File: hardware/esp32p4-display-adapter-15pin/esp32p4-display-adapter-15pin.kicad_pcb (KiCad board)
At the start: 2 copper layers, 20 x 30 mm, 0 parts

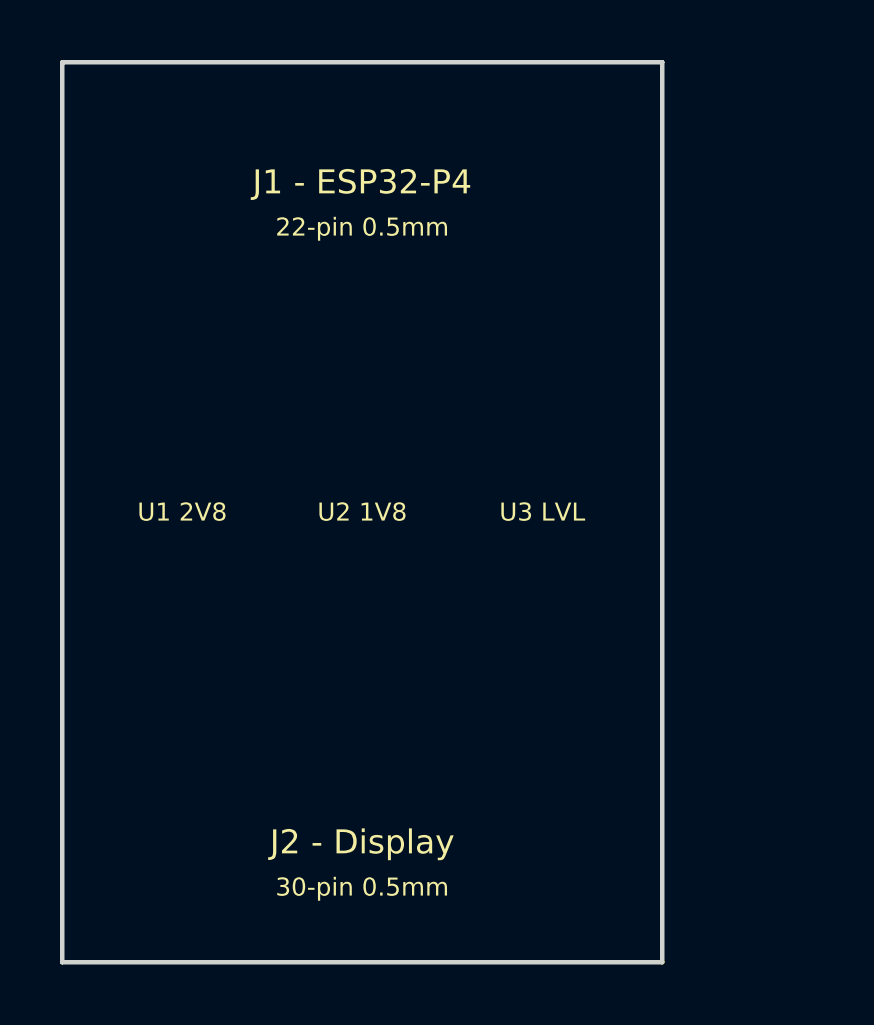
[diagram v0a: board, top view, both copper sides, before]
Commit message: Restore esp32p4-display-adapter (22-pin), add esp32p4-display-adapter-15pin
- esp32p4-display-adapter: 22-pin 0.5mm (your working version restored)
- esp32p4-display-adapter-15pin: NEW - 15-pin 1.0mm (same pinout as RPi)
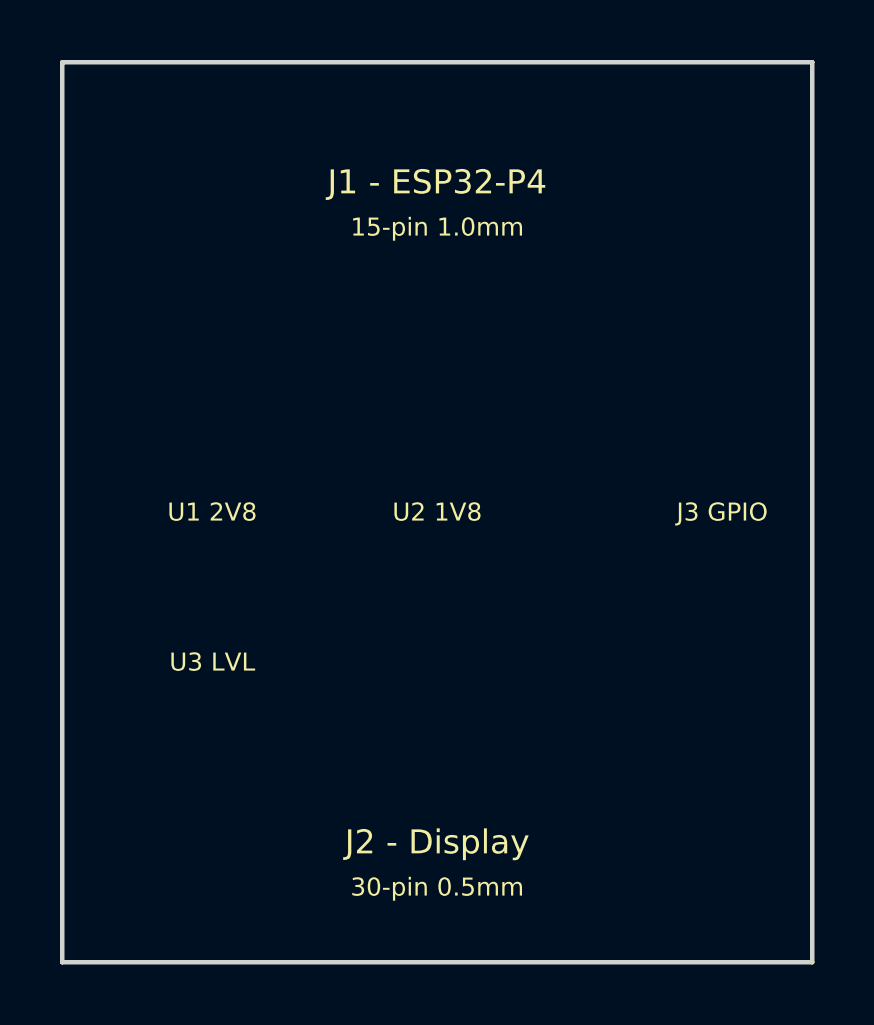
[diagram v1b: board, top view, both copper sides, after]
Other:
- board size 20 x 30 mm -> 25 x 30 mm
- board text added: "15-pin 1.0mm"
- board text added: "J3 GPIO"
- board text removed: "22-pin 0.5mm"
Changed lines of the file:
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@@
   (paper "A4")
   (title_block
-    (title "ESP32-P4 DSI to Round Display Adapter (22-pin)")
+    (title "ESP32-P4 DSI to Round Display Adapter (15-pin)")
     (date "2026-04-24")
     (rev "1.0")
@@
   (net 15 "TP_RESET_3V3")
   (net 16 "TP_RESET_1V8")
-  (net 17 "TP_INT")
-  (net 18 "LED_A")
-  (net 19 "LED_K")
   (gr_rect
     (start 0 0)
-    (end 20 30)
+    (end 25 30)
     (stroke (width 0.15) (type solid))
     (fill none)
@@
   )
   (gr_text "J1 - ESP32-P4"
-    (at 10 4 0)
+    (at 12.5 4 0)
     (layer "F.SilkS")
     (effects (font (size 0.8 0.8) (thickness 0.12)))
   )
-  (gr_text "22-pin 0.5mm"
-    (at 10 5.5 0)
+  (gr_text "15-pin 1.0mm"
+    (at 12.5 5.5 0)
     (layer "F.SilkS")
     (effects (font (size 0.6 0.6) (thickness 0.1)))
   )
   (gr_text "J2 - Display"
-    (at 10 26 0)
+    (at 12.5 26 0)
     (layer "F.SilkS")
     (effects (font (size 0.8 0.8) (thickness 0.12)))
   )
   (gr_text "30-pin 0.5mm"
-    (at 10 27.5 0)
+    (at 12.5 27.5 0)
+    (layer "F.SilkS")
+    (effects (font (size 0.6 0.6) (thickness 0.1)))
+  )
+  (gr_text "J3 GPIO"
+    (at 22 15 0)
     (layer "F.SilkS")
     (effects (font (size 0.6 0.6) (thickness 0.1)))
   )
   (gr_text "U1 2V8"
-    (at 4 15 0)
+    (at 5 15 0)
     (layer "F.SilkS")
     (effects (font (size 0.6 0.6) (thickness 0.1)))
   )
   (gr_text "U2 1V8"
-    (at 10 15 0)
+    (at 12.5 15 0)
     (layer "F.SilkS")
     (effects (font (size 0.6 0.6) (thickness 0.1)))
   )
   (gr_text "U3 LVL"
-    (at 16 15 0)
+    (at 5 20 0)
     (layer "F.SilkS")
     (effects (font (size 0.6 0.6) (thickness 0.1)))
   )
   (gr_text "MIPI: 100R diff"
-    (at 10 21 0)
+    (at 12.5 22 0)
     (layer "Cmts.User")
     (effects (font (size 0.6 0.6) (thickness 0.1)))
